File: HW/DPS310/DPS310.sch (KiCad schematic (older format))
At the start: 7 parts, among them J1 Screw_Terminal_01x05, U1 DPS310

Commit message: fix name
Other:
- note removed: "R3 select\nthe address to \n0x76 instead\nof 0x77."
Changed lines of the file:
@@
 EESchema Schematic File Version 4
-LIBS:DSP310-cache
+LIBS:DPS310-cache
 EELAYER 30 0
 EELAYER END
@@
 encoding utf-8
 Sheet 1 1
-Title "DSP310 Breakout is optional and will setthe address to 0x76 insteadDSP310"
+Title "Croquette DPS310 is optional and will setthe address to 0x76 insteadDSP310"
 Date "2020-01-10"
 Rev "1.0"
@@
 	1    0    0    -1
 $EndComp
-Text Notes 3705 3570 0    50   ~ 0
-R3 select\nthe address to \n0x76 instead\nof 0x77.
 Text Label 4110 3030 2    50   ~ 0
 INT

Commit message: PCB view
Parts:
- C1: footprint (none) -> Capacitor_SMD:C_0805_2012Metric_Pad1.15x1.40mm_HandSolder; symbol Device:C_Small -> DPS310-rescue:C_Small-Device
- J1: footprint (none) -> Connector_PinHeader_2.54mm:PinHeader_1x05_P2.54mm_Vertical; symbol Connector:Screw_Terminal_01x05 -> DPS310-rescue:Screw_Terminal_01x05-Connector
- JP1: footprint (none) -> Connector_PinHeader_2.54mm:PinHeader_1x02_P2.54mm_Vertical; symbol Device:Jumper_NO_Small -> DPS310-rescue:Jumper_NO_Small-Device
- R1, R2, R3: footprint (none) -> Resistor_SMD:R_0805_2012Metric_Pad1.15x1.40mm_HandSolder; symbol Device:R_Small -> DPS310-rescue:R_Small-Device
- U1: footprint (none) -> Package_LGA:Bosch_LGA-8_2x2.5mm_P0.65mm_ClockwisePinNumbering; symbol electroniccats:DPS310 -> DPS310-rescue:DPS310-electroniccats
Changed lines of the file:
@@
 $EndDescr
 $Comp
-L Device:R_Small R2
+L DPS310-rescue:R_Small-Device R2
 U 1 1 5E18C0AA
 P 4480 2630
 F 0 "R2" H 4539 2676 50  0000 L CNN
 F 1 "10K" H 4539 2585 50  0000 L CNN
-F 2 "" H 4480 2630 50  0001 C CNN
+F 2 "Resistor_SMD:R_0805_2012Metric_Pad1.15x1.40mm_HandSolder" H 4480 2630 50  0001 C CNN
 F 3 "~" H 4480 2630 50  0001 C CNN
 	1    4480 2630
@@
 $EndComp
 $Comp
-L Device:R_Small R1
+L DPS310-rescue:R_Small-Device R1
 U 1 1 5E18C4F8
 P 4230 2630
 F 0 "R1" H 4289 2676 50  0000 L CNN
 F 1 "10K" H 4289 2585 50  0000 L CNN
-F 2 "" H 4230 2630 50  0001 C CNN
+F 2 "Resistor_SMD:R_0805_2012Metric_Pad1.15x1.40mm_HandSolder" H 4230 2630 50  0001 C CNN
 F 3 "~" H 4230 2630 50  0001 C CNN
 	1    4230 2630
@@
 $EndComp
 $Comp
-L Device:R_Small R3
+L DPS310-rescue:R_Small-Device R3
 U 1 1 5E18C84B
 P 4320 3410
 F 0 "R3" H 4379 3456 50  0000 L CNN
 F 1 "100K" H 4379 3365 50  0000 L CNN
-F 2 "" H 4320 3410 50  0001 C CNN
+F 2 "Resistor_SMD:R_0805_2012Metric_Pad1.15x1.40mm_HandSolder" H 4320 3410 50  0001 C CNN
 F 3 "~" H 4320 3410 50  0001 C CNN
 	1    4320 3410
@@
 $EndComp
 $Comp
-L Device:C_Small C1
+L DPS310-rescue:C_Small-Device C1
 U 1 1 5E18CE72
 P 5910 2915
 F 0 "C1" H 6002 2961 50  0000 L CNN
 F 1 "C_Small" H 6002 2870 50  0000 L CNN
-F 2 "" H 5910 2915 50  0001 C CNN
+F 2 "Capacitor_SMD:C_0805_2012Metric_Pad1.15x1.40mm_HandSolder" H 5910 2915 50  0001 C CNN
 F 3 "~" H 5910 2915 50  0001 C CNN
 	1    5910 2915
@@
 	5910 3085 5915 3085
 $Comp
-L power:GND #PWR03
+L DPS310-rescue:GND-power #PWR03
 U 1 1 5E19C877
 P 5915 3085
@@
 $EndComp
 $Comp
-L power:VCC #PWR02
+L DPS310-rescue:VCC-power #PWR02
 U 1 1 5E19CE08
 P 5675 2635
@@
 	5600 3180 5600 3365
 $Comp
-L power:GND #PWR04
+L DPS310-rescue:GND-power #PWR04
 U 1 1 5E19D6EA
 P 5600 3365
@@
 	4615 3030 4320 3030
 $Comp
-L Device:Jumper_NO_Small JP1
+L DPS310-rescue:Jumper_NO_Small-Device JP1
 U 1 1 5E1A15E9
 P 4320 3160
 F 0 "JP1" V 4275 2980 50  0000 L CNN
 F 1 "Jumper" V 4335 2850 50  0000 L CNN
-F 2 "" H 4320 3160 50  0001 C CNN
+F 2 "Connector_PinHeader_2.54mm:PinHeader_1x02_P2.54mm_Vertical" H 4320 3160 50  0001 C CNN
 F 3 "~" H 4320 3160 50  0001 C CNN
 	1    4320 3160
@@
 	4320 3510 4320 3565
 $Comp
-L power:GND #PWR05
+L DPS310-rescue:GND-power #PWR05
 U 1 1 5E1A325C
 P 4320 3565
@@
 	4350 2485 4480 2485
 $Comp
-L power:VCC #PWR01
+L DPS310-rescue:VCC-power #PWR01
 U 1 1 5E1A4316
 P 4350 2445
@@
 INT
 $Comp
-L electroniccats:DPS310 U1
+L DPS310-rescue:DPS310-electroniccats U1
 U 1 1 5E19AD10
 P 5065 2880
 F 0 "U1" H 5065 3205 50  0000 C CNN
 F 1 "DPS310" H 5065 3114 50  0000 C CNN
-F 2 "" H 5065 2880 50  0001 C CNN
+F 2 "Package_LGA:Bosch_LGA-8_2x2.5mm_P0.65mm_ClockwisePinNumbering" H 5065 2880 50  0001 C CNN
 F 3 "" H 5065 2880 50  0001 C CNN
 	1    5065 2880
@@
 $EndComp
 $Comp
-L power:VCC #PWR06
+L DPS310-rescue:VCC-power #PWR06
 U 1 1 5E1966DD
 P 4520 4610
@@
 	4520 4645 4520 4610
 $Comp
-L power:GND #PWR07
+L DPS310-rescue:GND-power #PWR07
 U 1 1 5E1976B7
 P 4800 4645
@@
 NoConn ~ 4615 3180
 $Comp
-L Connector:Screw_Terminal_01x05 J1
+L DPS310-rescue:Screw_Terminal_01x05-Connector J1
 U 1 1 5E19C2FB
 P 4900 4370
 F 0 "J1" V 4864 4082 50  0000 R CNN
 F 1 "Screw_Terminal_01x05" V 4773 4082 50  0000 R CNN
-F 2 "" H 4900 4370 50  0001 C CNN
+F 2 "Connector_PinHeader_2.54mm:PinHeader_1x05_P2.54mm_Vertical" H 4900 4370 50  0001 C CNN
 F 3 "~" H 4900 4370 50  0001 C CNN
 	1    4900 4370

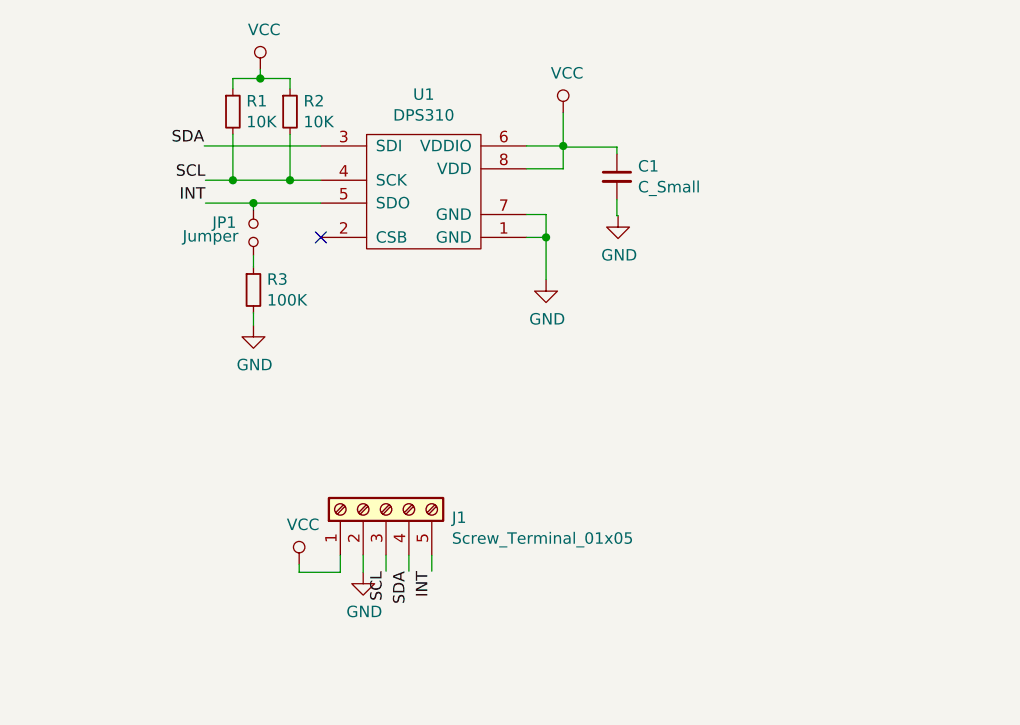
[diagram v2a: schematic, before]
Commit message: update for SPI and I2C support
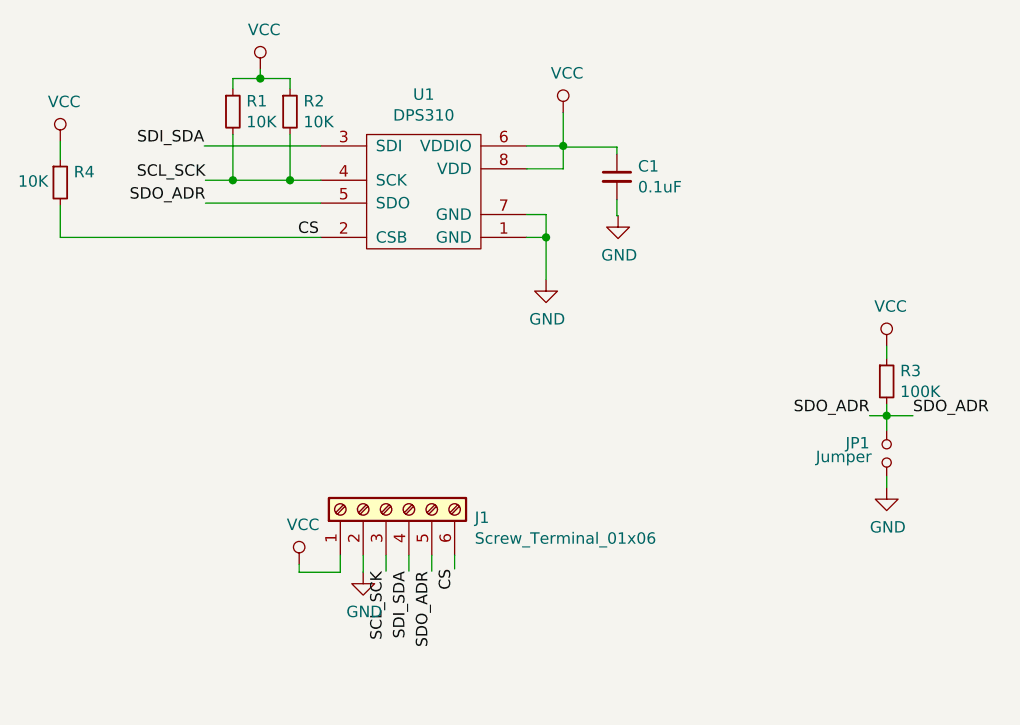
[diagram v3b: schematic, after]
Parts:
- removed J1: Screw_Terminal_01x05, Connector_PinHeader_2.54mm:PinHeader_1x05_P2.54mm_Vertical, symbol DPS310-rescue:Screw_Terminal_01x05-Connector
- added J1: Screw_Terminal_01x06, Connector_PinHeader_2.54mm:PinHeader_1x06_P2.54mm_Vertical, symbol Connector:Screw_Terminal_01x06
- added R4: 10K, Capacitor_SMD:C_0805_2012Metric_Pad1.15x1.40mm_HandSolder, symbol Device:R_Small
- C1: value C_Small -> 0.1uF
- JP1: footprint Connector_PinHeader_2.54mm:PinHeader_1x02_P2.54mm_Vertical -> Jumper:SolderJumper-2_P1.3mm_Open_TrianglePad1.0x1.5mm
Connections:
- net GND: now also JP1.2, J1.2 (Pin_2); no longer R3.2
- net VCC: now also R3.1, J1.1 (Pin_1), R4.1
- net CS: now reaches U1.2 (CSB)
- net CS: now also J1.6 (Pin_6), R4.2
- net INT renamed SDO_ADR
- net SDO_ADR: now also R3.2, J1.5 (Pin_5)
- net SCL renamed SCL_SCK
- net SCL_SCK: now also J1.3 (Pin_3)
- net SDA renamed SDI_SDA
- net SDI_SDA: now also J1.4 (Pin_4)
- no-connect marks 1 -> 0
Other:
- moved on the sheet: JP1, R3
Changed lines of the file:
@@
 EESchema Schematic File Version 4
-LIBS:DPS310-cache
 EELAYER 30 0
 EELAYER END
@@
 L DPS310-rescue:R_Small-Device R3
 U 1 1 5E18C84B
-P 4320 3410
-F 0 "R3" H 4379 3456 50  0000 L CNN
-F 1 "100K" H 4379 3365 50  0000 L CNN
-F 2 "Resistor_SMD:R_0805_2012Metric_Pad1.15x1.40mm_HandSolder" H 4320 3410 50  0001 C CNN
-F 3 "~" H 4320 3410 50  0001 C CNN
-	1    4320 3410
+P 7090 3810
+F 0 "R3" H 7149 3856 50  0000 L CNN
+F 1 "100K" H 7149 3765 50  0000 L CNN
+F 2 "Resistor_SMD:R_0805_2012Metric_Pad1.15x1.40mm_HandSolder" H 7090 3810 50  0001 C CNN
+F 3 "~" H 7090 3810 50  0001 C CNN
+	1    7090 3810
 	1    0    0    -1
 $EndComp
@@
 P 5910 2915
 F 0 "C1" H 6002 2961 50  0000 L CNN
-F 1 "C_Small" H 6002 2870 50  0000 L CNN
+F 1 "0.1uF" H 6002 2870 50  0000 L CNN
 F 2 "Capacitor_SMD:C_0805_2012Metric_Pad1.15x1.40mm_HandSolder" H 5910 2915 50  0001 C CNN
 F 3 "~" H 5910 2915 50  0001 C CNN
@@
 Connection ~ 4230 2930
 Text Label 4105 2780 2    50   ~ 0
-SDA
+SDI_SDA
 Text Label 4110 2930 2    50   ~ 0
-SCL
-Wire Wire Line
-	4615 3030 4320 3030
+SCL_SCK
 $Comp
 L DPS310-rescue:Jumper_NO_Small-Device JP1
 U 1 1 5E1A15E9
-P 4320 3160
-F 0 "JP1" V 4275 2980 50  0000 L CNN
-F 1 "Jumper" V 4335 2850 50  0000 L CNN
-F 2 "Connector_PinHeader_2.54mm:PinHeader_1x02_P2.54mm_Vertical" H 4320 3160 50  0001 C CNN
-F 3 "~" H 4320 3160 50  0001 C CNN
-	1    4320 3160
+P 7090 4125
+F 0 "JP1" V 7045 3945 50  0000 L CNN
+F 1 "Jumper" V 7105 3815 50  0000 L CNN
+F 2 "Jumper:SolderJumper-2_P1.3mm_Open_TrianglePad1.0x1.5mm" H 7090 4125 50  0001 C CNN
+F 3 "~" H 7090 4125 50  0001 C CNN
+	1    7090 4125
 	0    1    1    0
 $EndComp
 Wire Wire Line
-	4320 3060 4320 3030
-Connection ~ 4320 3030
-Wire Wire Line
-	4320 3030 4110 3030
-Wire Wire Line
-	4320 3260 4320 3310
-Wire Wire Line
-	4320 3510 4320 3565
+	7090 4225 7090 4275
 $Comp
 L DPS310-rescue:GND-power #PWR05
 U 1 1 5E1A325C
-P 4320 3565
-F 0 "#PWR05" H 4320 3315 50  0001 C CNN
-F 1 "GND" H 4325 3392 50  0000 C CNN
-F 2 "" H 4320 3565 50  0001 C CNN
-F 3 "" H 4320 3565 50  0001 C CNN
-	1    4320 3565
+P 7090 4275
+F 0 "#PWR05" H 7090 4025 50  0001 C CNN
+F 1 "GND" H 7095 4102 50  0000 C CNN
+F 2 "" H 7090 4275 50  0001 C CNN
+F 3 "" H 7090 4275 50  0001 C CNN
+	1    7090 4275
 	1    0    0    -1
 $EndComp
 Text Label 4110 3030 2    50   ~ 0
-INT
+SDO_ADR
 Wire Wire Line
 	4230 2530 4230 2485
@@
 	4700 4570 4700 4645
 Text Label 5000 4640 3    50   ~ 0
-SDA
+SDI_SDA
 Text Label 4900 4640 3    50   ~ 0
-SCL
+SCL_SCK
 Text Label 5100 4640 3    50   ~ 0
-INT
+SDO_ADR
 $Comp
 L DPS310-rescue:DPS310-electroniccats U1
@@
 	1    0    0    -1
 $EndComp
-NoConn ~ 4615 3180
-$Comp
-L DPS310-rescue:Screw_Terminal_01x05-Connector J1
-U 1 1 5E19C2FB
+Text Label 4515 3180 0    50   ~ 0
+CS
+$Comp
+L Connector:Screw_Terminal_01x06 J1
+U 1 1 5E40900C
 P 4900 4370
-F 0 "J1" V 4864 4082 50  0000 R CNN
-F 1 "Screw_Terminal_01x05" V 4773 4082 50  0000 R CNN
-F 2 "Connector_PinHeader_2.54mm:PinHeader_1x05_P2.54mm_Vertical" H 4900 4370 50  0001 C CNN
+F 0 "J1" V 4864 3982 50  0000 R CNN
+F 1 "Screw_Terminal_01x06" V 4773 3982 50  0000 R CNN
+F 2 "Connector_PinHeader_2.54mm:PinHeader_1x06_P2.54mm_Vertical" H 4900 4370 50  0001 C CNN
 F 3 "~" H 4900 4370 50  0001 C CNN
 	1    4900 4370
 	0    -1   -1   0
 $EndComp
+Wire Wire Line
+	5200 4570 5200 4630
+Text Label 5200 4630 3    50   ~ 0
+CS
+Wire Wire Line
+	4110 3030 4615 3030
+Wire Wire Line
+	7090 4025 7090 3960
+Wire Wire Line
+	7090 3710 7090 3655
+Wire Wire Line
+	7090 3960 7205 3960
+Connection ~ 7090 3960
+Wire Wire Line
+	7090 3960 7090 3910
+Wire Wire Line
+	7090 3960 7015 3960
+Text Label 7015 3960 2    50   ~ 0
+SDO_ADR
+Text Label 7205 3960 0    50   ~ 0
+SDO_ADR
+$Comp
+L power:VCC #PWR09
+U 1 1 5E411E48
+P 7090 3655
+F 0 "#PWR09" H 7090 3505 50  0001 C CNN
+F 1 "VCC" H 7107 3828 50  0000 C CNN
+F 2 "" H 7090 3655 50  0001 C CNN
+F 3 "" H 7090 3655 50  0001 C CNN
+	1    7090 3655
+	1    0    0    -1
+$EndComp
+Wire Wire Line
+	3475 3180 3475 3040
+Wire Wire Line
+	3475 3180 4615 3180
+$Comp
+L Device:R_Small R4
+U 1 1 5E4159C2
+P 3475 2940
+F 0 "R4" H 3534 2986 50  0000 L CNN
+F 1 "10K" H 3290 2945 50  0000 L CNN
+F 2 "Capacitor_SMD:C_0805_2012Metric_Pad1.15x1.40mm_HandSolder" H 3475 2940 50  0001 C CNN
+F 3 "~" H 3475 2940 50  0001 C CNN
+	1    3475 2940
+	1    0    0    -1
+$EndComp
+Wire Wire Line
+	3475 2840 3475 2760
+$Comp
+L power:VCC #PWR08
+U 1 1 5E417779
+P 3475 2760
+F 0 "#PWR08" H 3475 2610 50  0001 C CNN
+F 1 "VCC" H 3492 2933 50  0000 C CNN
+F 2 "" H 3475 2760 50  0001 C CNN
+F 3 "" H 3475 2760 50  0001 C CNN
+	1    3475 2760
+	1    0    0    -1
+$EndComp
 $EndSCHEMATC

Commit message: New Last  Revision
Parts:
- J1: symbol Connector:Screw_Terminal_01x06 -> DPS310-rescue:Screw_Terminal_01x06-Connector
- R4: symbol Device:R_Small -> DPS310-rescue:R_Small-Device
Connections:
- net SCL_SCK: no longer R2.2
- net SDI_SDA: now also R2.2
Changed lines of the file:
@@
 EESchema Schematic File Version 4
+LIBS:DPS310-cache
 EELAYER 30 0
 EELAYER END
@@
 $EndComp
 Wire Wire Line
-	4615 2930 4480 2930
-Wire Wire Line
-	4480 2730 4480 2930
-Connection ~ 4480 2930
-Wire Wire Line
 	4230 2930 4230 2730
 Wire Wire Line
-	4230 2930 4480 2930
-Wire Wire Line
-	4105 2780 4615 2780
+	4105 2780 4480 2780
 Wire Wire Line
 	4230 2930 4110 2930
@@
 CS
 $Comp
-L Connector:Screw_Terminal_01x06 J1
+L DPS310-rescue:Screw_Terminal_01x06-Connector J1
 U 1 1 5E40900C
 P 4900 4370
@@
 SDO_ADR
 $Comp
-L power:VCC #PWR09
+L DPS310-rescue:VCC-power #PWR09
 U 1 1 5E411E48
 P 7090 3655
@@
 	3475 3180 4615 3180
 $Comp
-L Device:R_Small R4
+L DPS310-rescue:R_Small-Device R4
 U 1 1 5E4159C2
 P 3475 2940
@@
 	3475 2840 3475 2760
 $Comp
-L power:VCC #PWR08
+L DPS310-rescue:VCC-power #PWR08
 U 1 1 5E417779
 P 3475 2760
@@
 	1    0    0    -1
 $EndComp
+Wire Wire Line
+	4230 2930 4615 2930
+Wire Wire Line
+	4480 2730 4480 2780
+Connection ~ 4480 2780
+Wire Wire Line
+	4480 2780 4615 2780
 $EndSCHEMATC

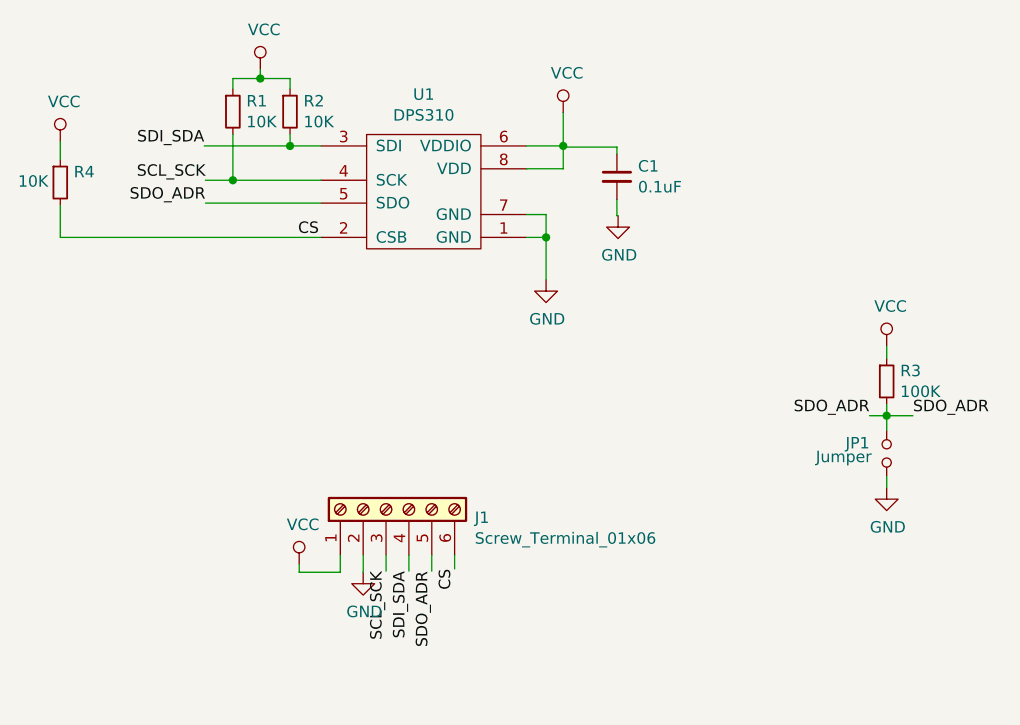
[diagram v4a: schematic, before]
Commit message: fix cap and traces
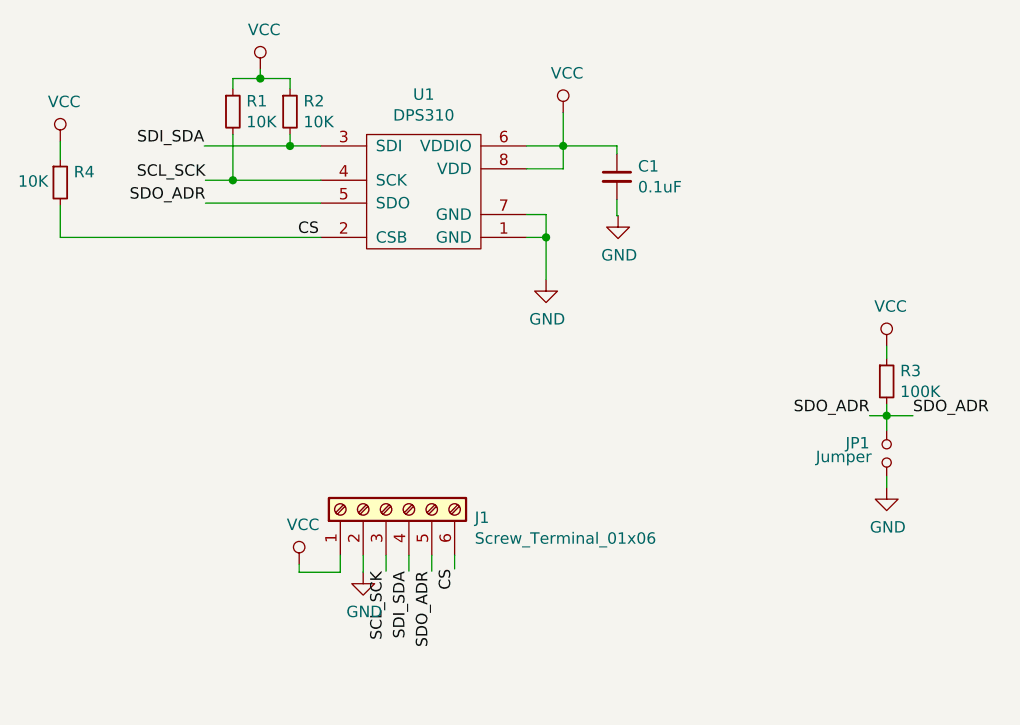
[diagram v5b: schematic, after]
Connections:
- net VCC: now also C1.1
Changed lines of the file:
@@
 EESchema Schematic File Version 4
-LIBS:DPS310-cache
 EELAYER 30 0
 EELAYER END
@@
 $EndComp
 Wire Wire Line
-	5515 2780 5675 2780
-Wire Wire Line
-	5675 2780 5675 2635
-Wire Wire Line
 	5515 2880 5675 2880
-Wire Wire Line
-	5675 2880 5675 2780
-Connection ~ 5675 2780
-Wire Wire Line
-	5680 2785 5910 2785
-Wire Wire Line
-	5910 2785 5910 2815
 Wire Wire Line
 	5910 3015 5910 3085
@@
 Wire Wire Line
 	4480 2780 4615 2780
+Wire Wire Line
+	5675 2635 5675 2780
+Wire Wire Line
+	5515 2780 5675 2780
+Connection ~ 5675 2780
+Wire Wire Line
+	5675 2780 5675 2880
+Wire Wire Line
+	5910 2780 5675 2780
+Wire Wire Line
+	5910 2780 5910 2815
 $EndSCHEMATC
